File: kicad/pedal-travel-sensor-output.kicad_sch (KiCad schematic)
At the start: 21 parts

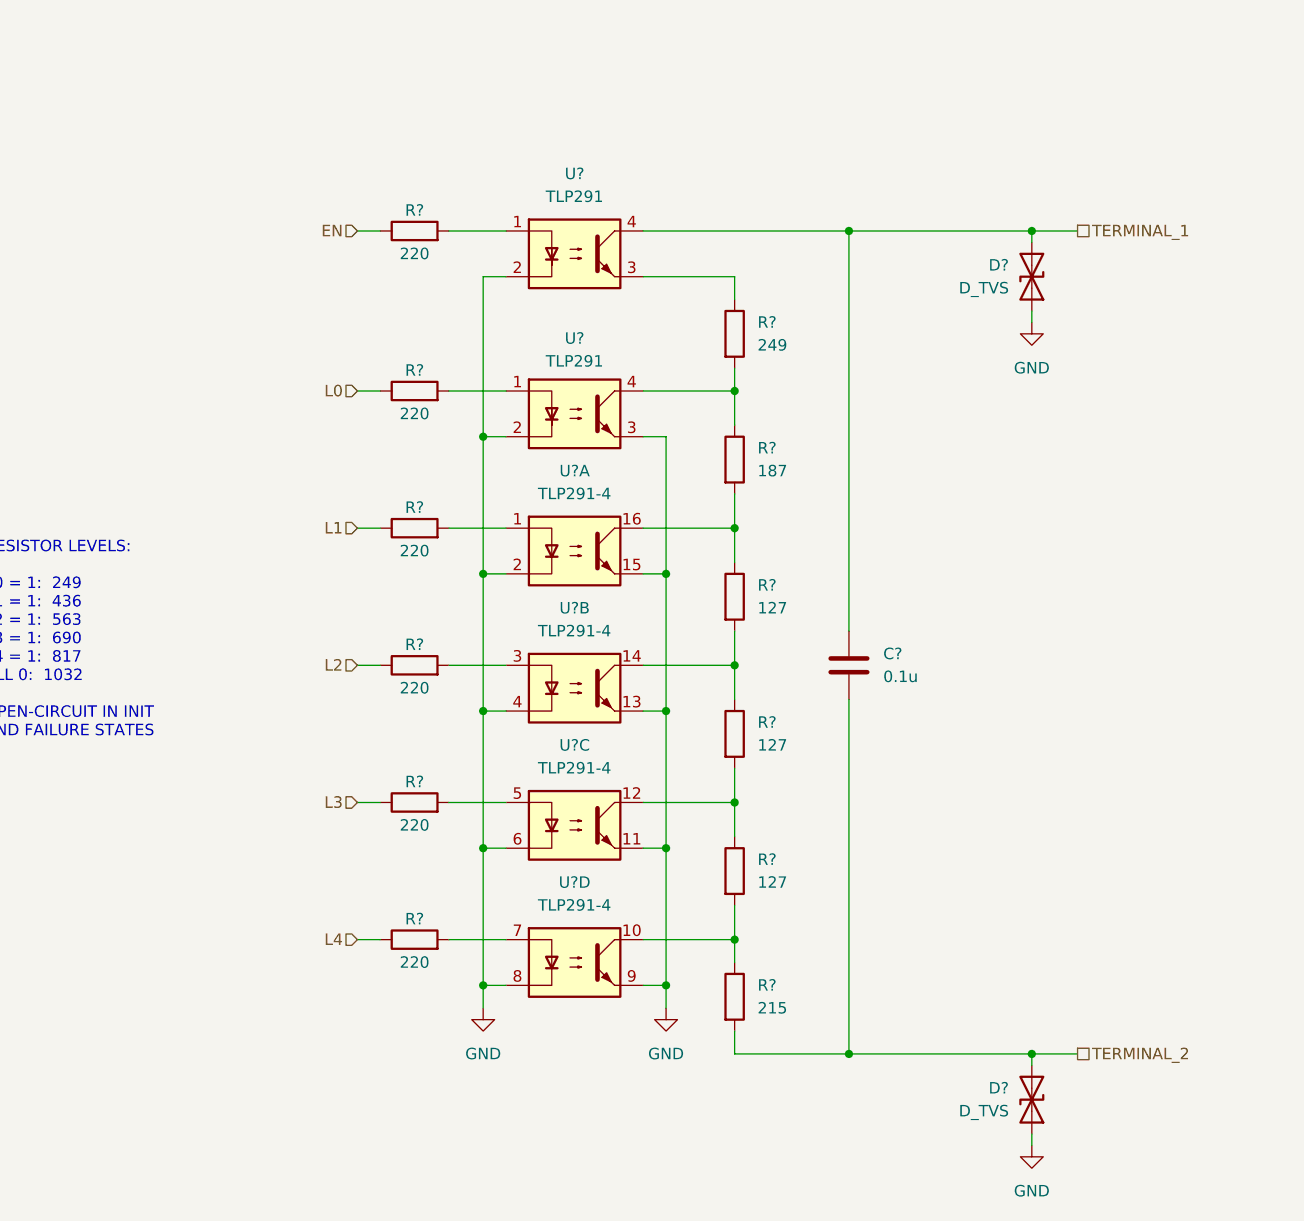
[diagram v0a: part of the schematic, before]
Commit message: Update pedal travel output
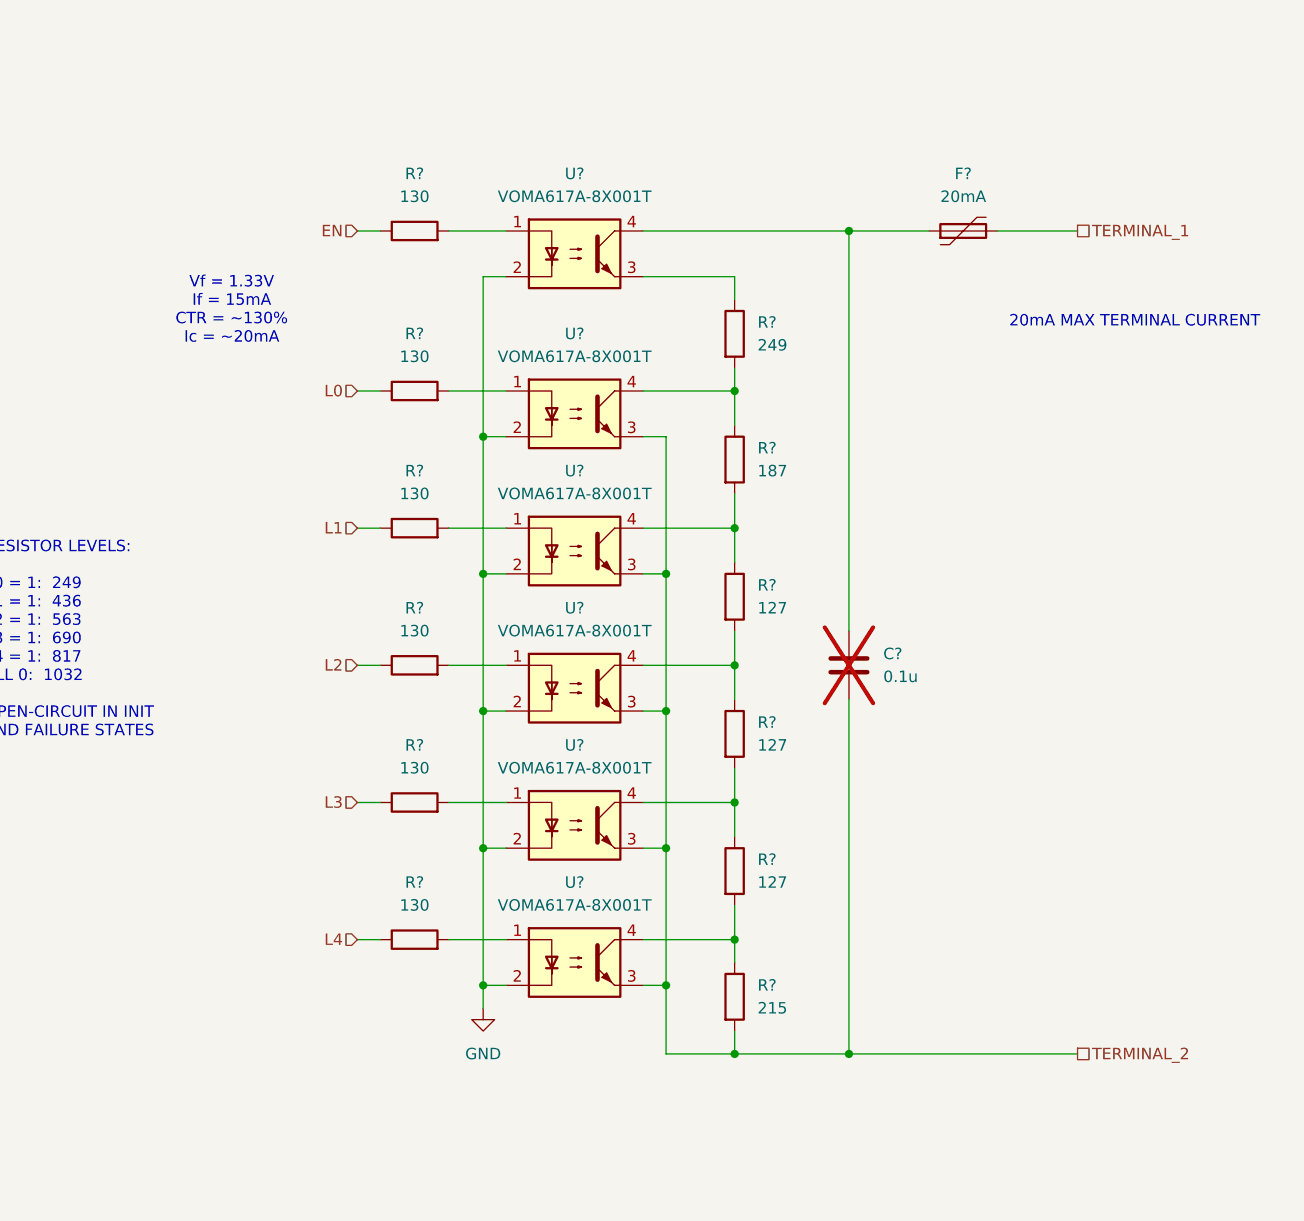
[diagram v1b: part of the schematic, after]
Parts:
- removed D? (x2): D_TVS, symbol symbols:D_TVS
- removed R? (x5): 220, symbol symbols:R
- removed U? (x4): TLP291-4, Package_SO:SOIC-16_4.55x10.3mm_P1.27mm, symbol symbols:TLP291-4
- removed U? (x2): TLP291, Package_SO:SOIC-4_4.55x2.6mm_P1.27mm, symbol symbols:TLP291
- added F?: 20mA, Fuse:Fuse_0603_1608Metric, symbol symbols:Polyfuse
- added R? (x5): 130, symbol symbols:R
- added U? (x6): VOMA617A-8X001T, symbol symbols:Optocoupler_DC_PhotoNPN_AKEC
- C?: now not fitted
- R?: value 220 -> 130
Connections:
- net GND: now also U?.2, U?.2, U?.2, U?.2, U?.2, U?.2
- net L0: now also R?.1
- net L1: now also R?.1
- net L2: now also R?.1
- net L3: now also R?.1
- net L4: now also R?.1
- net TERMINAL_1: now also F?.2; no longer C?.1
- net TERMINAL_2: now also U?.3, U?.3, U?.3, U?.3, U?.3
- net at R?.1, R?.2: now also U?.4 (x5)
- net at R?.2: now also U?.1
- net at R?.1: now also U?.3
- new net: C?.1, F?.1, U?.4
- new net: R?.2, U?.1 (x5)
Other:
- note added: "20mA MAX TERMINAL CURRENT"
- note added: "Vf = 1.33V If = 15mA CTR = ~130% Ic = ~20mA"

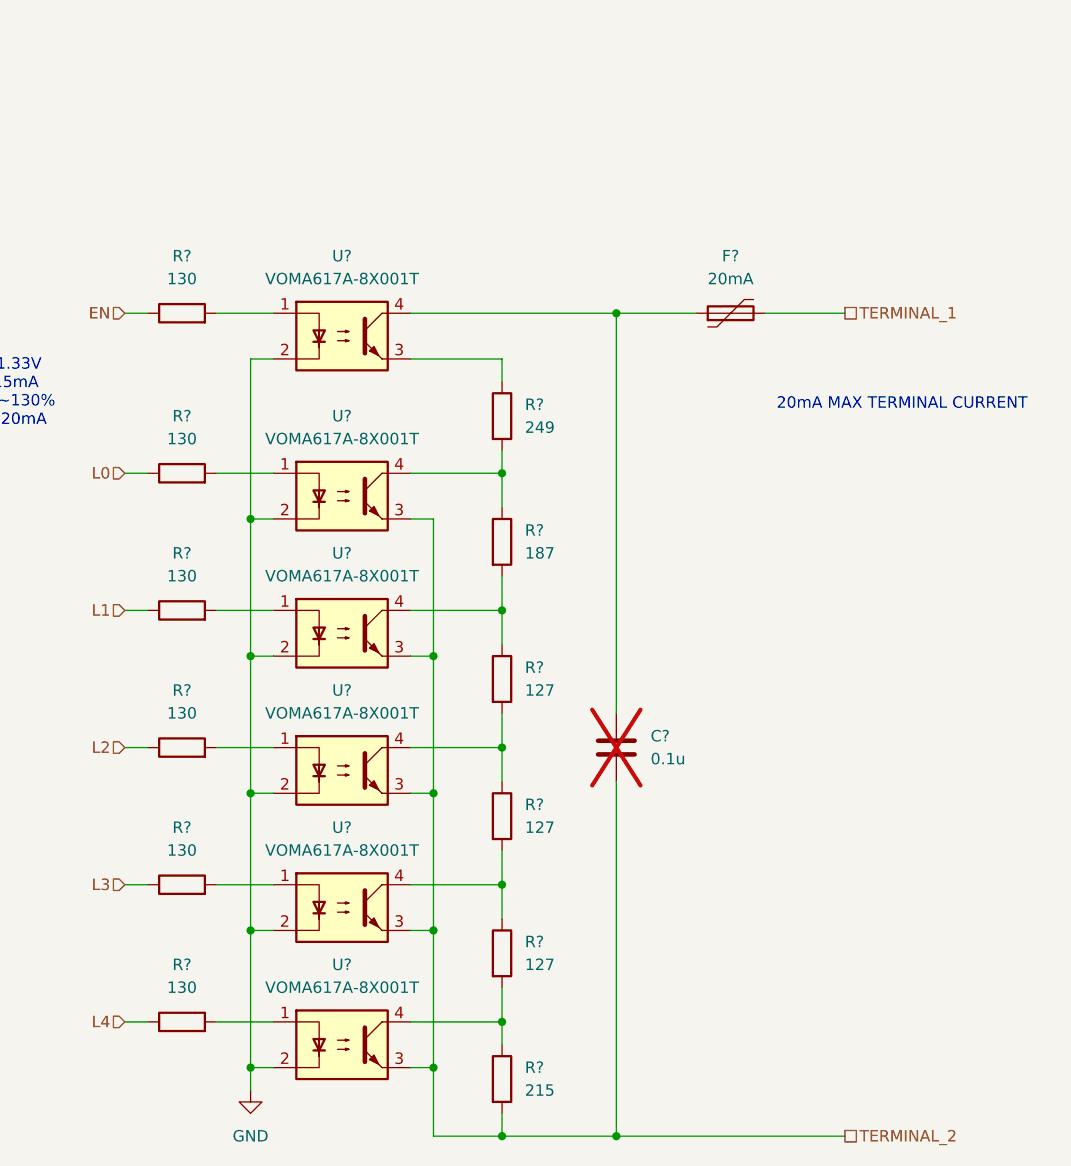
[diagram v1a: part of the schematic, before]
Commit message: Update connector; annotate and assign footprints
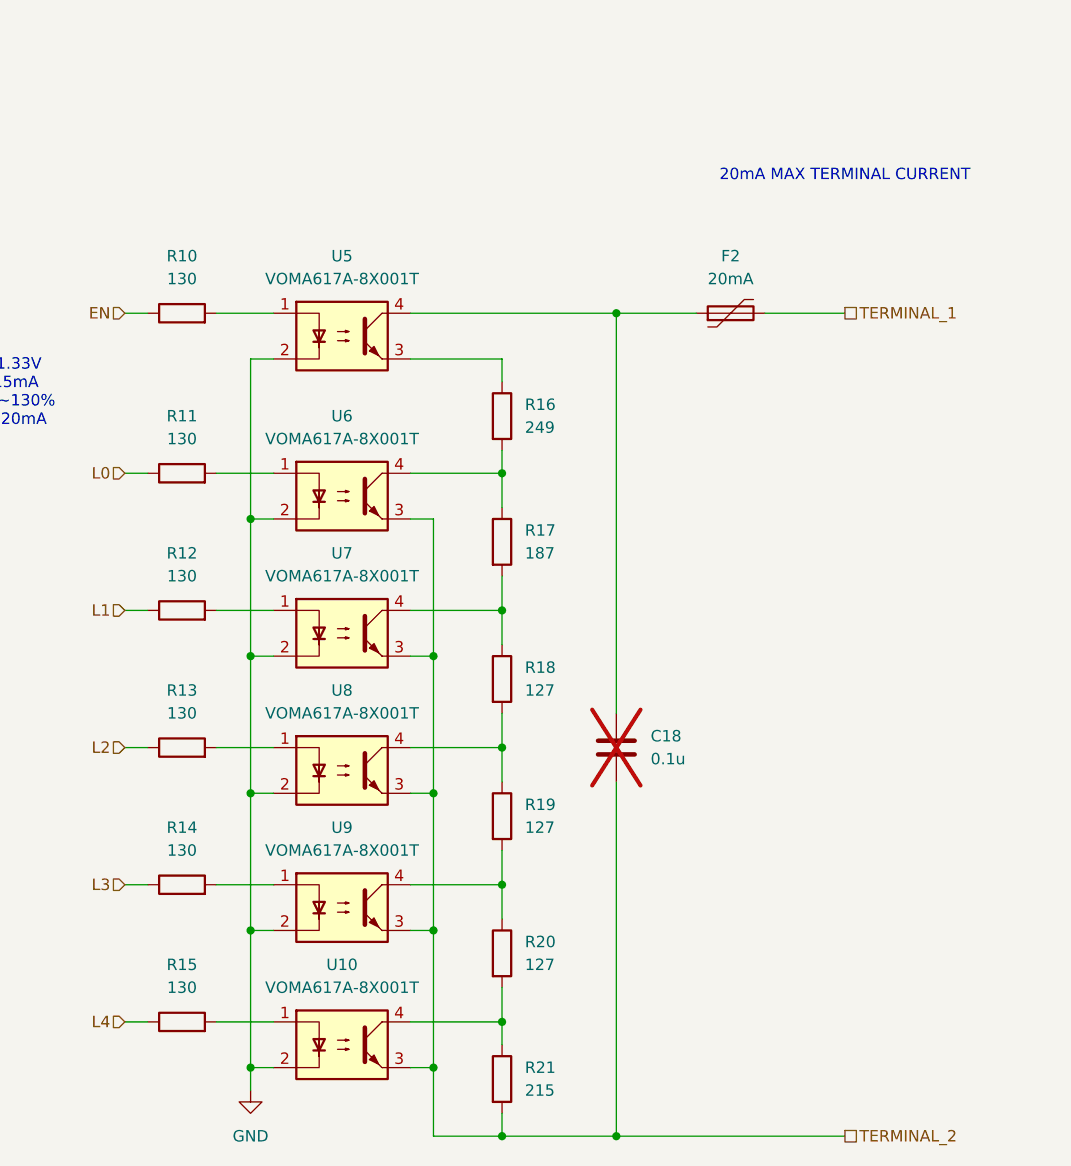
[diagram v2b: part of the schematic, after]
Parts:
- C18: renamed from C?; footprint (none) -> Capacitor_SMD:C_0603_1608Metric
- R10, R11, R12, R13, R14, R15, R16, R17, R18, R19, R20, R21: renamed from R?; footprint (none) -> Resistor_SMD:R_0603_1608Metric
- gave numbers to parts that had none: 7
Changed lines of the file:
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@@
 	(text "20mA MAX TERMINAL CURRENT"
 		(exclude_from_sim no)
-		(at 222.25 96.52 0)
+		(at 215.9 71.12 0)
 		(effects
 			(font
@@
 		(dnp no)
 		(fields_autoplaced yes)
-		(property "Reference" "U?"
+		(property "Reference" "U5"
 			(at 160.02 80.01 0)
 			(show_name no)
@@
 			(project "bmw-e36-abs-adapter"
 				(path "/325be93f-b4a6-4f2b-83c3-2ccd33e5cc03/3e268bd5-2ae2-4112-b445-da0f11812250"
-					(reference "U?")
+					(reference "U5")
 					(unit 1)
 				)
@@
 		(dnp no)
 		(fields_autoplaced yes)
-		(property "Reference" "F?"
+		(property "Reference" "F2"
 			(at 203.2 80.01 90)
 			(show_name no)
@@
 			(project "bmw-e36-abs-adapter"
 				(path "/325be93f-b4a6-4f2b-83c3-2ccd33e5cc03/3e268bd5-2ae2-4112-b445-da0f11812250"
-					(reference "F?")
+					(reference "F2")
 					(unit 1)
 				)
@@
 		(dnp no)
 		(fields_autoplaced yes)
-		(property "Reference" "#PWR?"
+		(property "Reference" "#PWR036"
 			(at 149.86 179.07 0)
 			(hide yes)
@@
 			(project "bmw-e36-abs-adapter"
 				(path "/325be93f-b4a6-4f2b-83c3-2ccd33e5cc03/3e268bd5-2ae2-4112-b445-da0f11812250"
-					(reference "#PWR?")
+					(reference "#PWR036")
 					(unit 1)
 				)
@@
 		(dnp no)
 		(fields_autoplaced yes)
-		(property "Reference" "R?"
+		(property "Reference" "R21"
 			(at 180.34 170.1799 0)
 			(show_name no)
@@
 			)
 		)
-		(property "Footprint" ""
+		(property "Footprint" "Resistor_SMD:R_0603_1608Metric"
 			(at 176.022 171.45 90)
 			(hide yes)
@@
 			(project "bmw-e36-abs-adapter"
 				(path "/325be93f-b4a6-4f2b-83c3-2ccd33e5cc03/3e268bd5-2ae2-4112-b445-da0f11812250"
-					(reference "R?")
+					(reference "R21")
 					(unit 1)
 				)
@@
 		(dnp no)
 		(fields_autoplaced yes)
-		(property "Reference" "R?"
+		(property "Reference" "R17"
 			(at 180.34 110.4899 0)
 			(show_name no)
@@
 			)
 		)
-		(property "Footprint" ""
+		(property "Footprint" "Resistor_SMD:R_0603_1608Metric"
 			(at 176.022 111.76 90)
 			(hide yes)
@@
 			(project "bmw-e36-abs-adapter"
 				(path "/325be93f-b4a6-4f2b-83c3-2ccd33e5cc03/3e268bd5-2ae2-4112-b445-da0f11812250"
-					(reference "R?")
+					(reference "R17")
 					(unit 1)
 				)
@@
 		(dnp no)
 		(fields_autoplaced yes)
-		(property "Reference" "R?"
+		(property "Reference" "R11"
 			(at 142.24 97.79 90)
 			(show_name no)
@@
 			)
 		)
-		(property "Footprint" ""
+		(property "Footprint" "Resistor_SMD:R_0603_1608Metric"
 			(at 142.24 105.918 90)
 			(hide yes)
@@
 			(project "bmw-e36-abs-adapter"
 				(path "/325be93f-b4a6-4f2b-83c3-2ccd33e5cc03/3e268bd5-2ae2-4112-b445-da0f11812250"
-					(reference "R?")
+					(reference "R11")
 					(unit 1)
 				)
@@
 		(dnp no)
 		(fields_autoplaced yes)
-		(property "Reference" "R?"
+		(property "Reference" "R18"
 			(at 180.34 125.7299 0)
 			(show_name no)
@@
 			)
 		)
-		(property "Footprint" ""
+		(property "Footprint" "Resistor_SMD:R_0603_1608Metric"
 			(at 176.022 127 90)
 			(hide yes)
@@
 			(project "bmw-e36-abs-adapter"
 				(path "/325be93f-b4a6-4f2b-83c3-2ccd33e5cc03/3e268bd5-2ae2-4112-b445-da0f11812250"
-					(reference "R?")
+					(reference "R18")
 					(unit 1)
 				)
@@
 		(dnp no)
 		(fields_autoplaced yes)
-		(property "Reference" "R?"
+		(property "Reference" "R19"
 			(at 180.34 140.9699 0)
 			(show_name no)
@@
 			)
 		)
-		(property "Footprint" ""
+		(property "Footprint" "Resistor_SMD:R_0603_1608Metric"
 			(at 176.022 142.24 90)
 			(hide yes)
@@
 			(project "bmw-e36-abs-adapter"
 				(path "/325be93f-b4a6-4f2b-83c3-2ccd33e5cc03/3e268bd5-2ae2-4112-b445-da0f11812250"
-					(reference "R?")
+					(reference "R19")
 					(unit 1)
 				)
@@
 		(dnp no)
 		(fields_autoplaced yes)
-		(property "Reference" "U?"
+		(property "Reference" "U10"
 			(at 160.02 158.75 0)
 			(show_name no)
@@
 			(project "bmw-e36-abs-adapter"
 				(path "/325be93f-b4a6-4f2b-83c3-2ccd33e5cc03/3e268bd5-2ae2-4112-b445-da0f11812250"
-					(reference "U?")
+					(reference "U10")
 					(unit 1)
 				)
@@
 		(dnp no)
 		(fields_autoplaced yes)
-		(property "Reference" "U?"
+		(property "Reference" "U7"
 			(at 160.02 113.03 0)
 			(show_name no)
@@
 			(project "bmw-e36-abs-adapter"
 				(path "/325be93f-b4a6-4f2b-83c3-2ccd33e5cc03/3e268bd5-2ae2-4112-b445-da0f11812250"
-					(reference "U?")
+					(reference "U7")
 					(unit 1)
 				)
@@
 		(dnp no)
 		(fields_autoplaced yes)
-		(property "Reference" "U?"
+		(property "Reference" "U9"
 			(at 160.02 143.51 0)
 			(show_name no)
@@
 			(project "bmw-e36-abs-adapter"
 				(path "/325be93f-b4a6-4f2b-83c3-2ccd33e5cc03/3e268bd5-2ae2-4112-b445-da0f11812250"
-					(reference "U?")
+					(reference "U9")
 					(unit 1)
 				)
@@
 		(dnp no)
 		(fields_autoplaced yes)
-		(property "Reference" "R?"
+		(property "Reference" "R16"
 			(at 180.34 96.5199 0)
 			(show_name no)
@@
 			)
 		)
-		(property "Footprint" ""
+		(property "Footprint" "Resistor_SMD:R_0603_1608Metric"
 			(at 176.022 97.79 90)
 			(hide yes)
@@
 			(project "bmw-e36-abs-adapter"
 				(path "/325be93f-b4a6-4f2b-83c3-2ccd33e5cc03/3e268bd5-2ae2-4112-b445-da0f11812250"
-					(reference "R?")
+					(reference "R16")
 					(unit 1)
 				)
@@
 		(dnp no)
 		(fields_autoplaced yes)
-		(property "Reference" "U?"
+		(property "Reference" "U6"
 			(at 160.02 97.79 0)
 			(show_name no)
@@
 			(project "bmw-e36-abs-adapter"
 				(path "/325be93f-b4a6-4f2b-83c3-2ccd33e5cc03/3e268bd5-2ae2-4112-b445-da0f11812250"
-					(reference "U?")
+					(reference "U6")
 					(unit 1)
 				)
@@
 		(dnp no)
 		(fields_autoplaced yes)
-		(property "Reference" "R?"
+		(property "Reference" "R14"
 			(at 142.24 143.51 90)
 			(show_name no)
@@
 			)
 		)
-		(property "Footprint" ""
+		(property "Footprint" "Resistor_SMD:R_0603_1608Metric"
 			(at 142.24 151.638 90)
 			(hide yes)
@@
 			(project "bmw-e36-abs-adapter"
 				(path "/325be93f-b4a6-4f2b-83c3-2ccd33e5cc03/3e268bd5-2ae2-4112-b445-da0f11812250"
-					(reference "R?")
+					(reference "R14")
 					(unit 1)
 				)
@@
 		(dnp no)
 		(fields_autoplaced yes)
-		(property "Reference" "U?"
+		(property "Reference" "U8"
 			(at 160.02 128.27 0)
 			(show_name no)
@@
 			(project "bmw-e36-abs-adapter"
 				(path "/325be93f-b4a6-4f2b-83c3-2ccd33e5cc03/3e268bd5-2ae2-4112-b445-da0f11812250"
-					(reference "U?")
+					(reference "U8")
 					(unit 1)
 				)
@@
 		(dnp no)
 		(fields_autoplaced yes)
-		(property "Reference" "R?"
+		(property "Reference" "R13"
 			(at 142.24 128.27 90)
 			(show_name no)
@@
 			)
 		)
-		(property "Footprint" ""
+		(property "Footprint" "Resistor_SMD:R_0603_1608Metric"
 			(at 142.24 136.398 90)
 			(hide yes)
@@
 			(project "bmw-e36-abs-adapter"
 				(path "/325be93f-b4a6-4f2b-83c3-2ccd33e5cc03/3e268bd5-2ae2-4112-b445-da0f11812250"
-					(reference "R?")
+					(reference "R13")
 					(unit 1)
 				)
@@
 		(dnp no)
 		(fields_autoplaced yes)
-		(property "Reference" "R?"
+		(property "Reference" "R20"
 			(at 180.34 156.2099 0)
 			(show_name no)
@@
 			)
 		)
-		(property "Footprint" ""
+		(property "Footprint" "Resistor_SMD:R_0603_1608Metric"
 			(at 176.022 157.48 90)
 			(hide yes)
@@
 			(project "bmw-e36-abs-adapter"
 				(path "/325be93f-b4a6-4f2b-83c3-2ccd33e5cc03/3e268bd5-2ae2-4112-b445-da0f11812250"
-					(reference "R?")
+					(reference "R20")
 					(unit 1)
 				)
@@
 		(dnp no)
 		(fields_autoplaced yes)
-		(property "Reference" "R?"
+		(property "Reference" "R12"
 			(at 142.24 113.03 90)
 			(show_name no)
@@
 			)
 		)
-		(property "Footprint" ""
+		(property "Footprint" "Resistor_SMD:R_0603_1608Metric"
 			(at 142.24 121.158 90)
 			(hide yes)
@@
 			(project "bmw-e36-abs-adapter"
 				(path "/325be93f-b4a6-4f2b-83c3-2ccd33e5cc03/3e268bd5-2ae2-4112-b445-da0f11812250"
-					(reference "R?")
+					(reference "R12")
 					(unit 1)
 				)
@@
 		(dnp no)
 		(fields_autoplaced yes)
-		(property "Reference" "R?"
+		(property "Reference" "R15"
 			(at 142.24 158.75 90)
 			(show_name no)
@@
 			)
 		)
-		(property "Footprint" ""
+		(property "Footprint" "Resistor_SMD:R_0603_1608Metric"
 			(at 142.24 166.878 90)
 			(hide yes)
@@
 			(project "bmw-e36-abs-adapter"
 				(path "/325be93f-b4a6-4f2b-83c3-2ccd33e5cc03/3e268bd5-2ae2-4112-b445-da0f11812250"
-					(reference "R?")
+					(reference "R15")
 					(unit 1)
 				)
@@
 		(dnp yes)
 		(fields_autoplaced yes)
-		(property "Reference" "C?"
+		(property "Reference" "C18"
 			(at 194.31 133.3499 0)
 			(show_name no)
@@
 			)
 		)
-		(property "Footprint" ""
+		(property "Footprint" "Capacitor_SMD:C_0603_1608Metric"
 			(at 191.4652 138.43 0)
 			(hide yes)
@@
 			(project "bmw-e36-abs-adapter"
 				(path "/325be93f-b4a6-4f2b-83c3-2ccd33e5cc03/3e268bd5-2ae2-4112-b445-da0f11812250"
-					(reference "C?")
+					(reference "C18")
 					(unit 1)
 				)
@@
 		(dnp no)
 		(fields_autoplaced yes)
-		(property "Reference" "R?"
+		(property "Reference" "R10"
 			(at 142.24 80.01 90)
 			(show_name no)
@@
 			)
 		)
-		(property "Footprint" ""
+		(property "Footprint" "Resistor_SMD:R_0603_1608Metric"
 			(at 142.24 88.138 90)
 			(hide yes)
@@
 			(project "bmw-e36-abs-adapter"
 				(path "/325be93f-b4a6-4f2b-83c3-2ccd33e5cc03/3e268bd5-2ae2-4112-b445-da0f11812250"
-					(reference "R?")
+					(reference "R10")
 					(unit 1)
 				)
